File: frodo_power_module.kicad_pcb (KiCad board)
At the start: 2 copper layers, 55 x 71.2 mm, 39 parts, among them J1 Keystone 1098, J10 SWD Header, J2 Molex MicroFit 2x2, J3 Molex MicroFit 2x2, J4 Molex MicroFit 2x2, J5 Molex MicroFit 2x2, J6 Molex MicroFit 2x2, J7 JST-GH, J8 JST-GH, J9 JST-GH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

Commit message: Update PCB
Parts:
- removed SW1, SW2: EVQ-PUC02K, Button_Switch_SMD:Panasonic_EVQPUL_EVQPUC
- added C12: 1u, Capacitor_SMD:C_0805_2012Metric, B.Cu at (124.5, 114.5)
- added C13: 1u, Capacitor_SMD:C_0805_2012Metric, B.Cu at (124.5, 117.5)
- added C14: 100n, Capacitor_SMD:C_0603_1608Metric, B.Cu at (133.0, 114.2)
- added C15: 100n, Capacitor_SMD:C_0603_1608Metric, B.Cu at (133.0, 116.8)
- added C16: 100n, Capacitor_SMD:C_0603_1608Metric, B.Cu at (133.0, 119.3)
- added C17: 100n, Capacitor_SMD:C_0603_1608Metric, B.Cu at (133.0, 121.8)
- added JP1: SolderJumper_2_Open, Jumper:SolderJumper-2_P1.3mm_Open_RoundedPad1.0x1.5mm, B.Cu at (128.8, 114.8)
- added JP2: SolderJumper_2_Open, Jumper:SolderJumper-2_P1.3mm_Open_RoundedPad1.0x1.5mm, B.Cu at (128.8, 118.3)
- added JP3: SolderJumper_2_Open, Jumper:SolderJumper-2_P1.3mm_Open_RoundedPad1.0x1.5mm, B.Cu at (128.8, 121.9)
- added R10: 0, Resistor_SMD:R_0603_1608Metric, B.Cu at (110.3, 109.0)
- added R11: 10k, Resistor_SMD:R_0603_1608Metric, B.Cu at (110.3, 111.5)
- added R12: 10k, Resistor_SMD:R_0603_1608Metric, B.Cu at (110.3, 114.0)
- added R13: TODO, Resistor_SMD:R_2512_6332Metric, B.Cu at (110.3, 116.5)
- added R14: 100, Resistor_SMD:R_0603_1608Metric, B.Cu at (110.3, 119.0)
- added R15: 160, Resistor_SMD:R_0603_1608Metric, B.Cu at (106.3, 109.0)
- added R16: 260, Resistor_SMD:R_0603_1608Metric, B.Cu at (106.3, 111.5)
- added R17: 100, Resistor_SMD:R_0603_1608Metric, B.Cu at (106.3, 114.0)
- added R5: 100k, Resistor_SMD:R_0603_1608Metric, B.Cu at (114.3, 109.0)
- added R6: 4.7k, Resistor_SMD:R_0603_1608Metric, B.Cu at (114.3, 111.5)
- added R7: 1k, Resistor_SMD:R_0603_1608Metric, B.Cu at (114.3, 114.0)
- added R8: 1k, Resistor_SMD:R_0603_1608Metric, B.Cu at (114.3, 116.5)
- added R9: DNP, Resistor_SMD:R_0603_1608Metric, B.Cu at (114.3, 119.0)
- added TH1: NCU18XH103F6SRB, Resistor_SMD:R_0603_1608Metric, B.Cu at (133.0, 124.3)
- H1, H2, H3, H4: value MountingHole_3.2mm_M3_Pad_Via -> MountingHole_Pad
- moved C7 14.6 mm to (110.0, 134.0)
- moved U1 11.9 mm to (146.2, 109.6)
- moved U5 10.8 mm to (140.0, 136.8)
- moved C8 8.32 mm to (118.8, 109.5)
- moved C10 8.32 mm to (118.8, 114.5)
- moved C11 8.32 mm to (118.8, 117.0)
- moved C9 8.32 mm to (118.8, 112.0)
- moved L1 8.32 mm to (118.8, 119.5)
- moved R3 8.32 mm to (118.8, 122.0)
- moved R4 8.32 mm to (118.8, 124.5)
- moved Y1 6.37 mm to (139.2, 129.3)
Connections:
- net +12V renamed VDC
- C1 pad 2: +BATT -> +VSW
- H1 pad 1: (no net) -> GND
- H2 pad 1: (no net) -> GND
- H3 pad 1: (no net) -> GND
- H4 pad 1: (no net) -> GND
- J1 pad 1: +BATT -> BATT_RAW
- U2 pad 1: +BATT -> +VSW
- U4 pad 1: unconnected-(U4-IN-Pad1) -> Net-(D1-K)
- U4 pad 10: unconnected-(U4-OUT-Pad10) -> +BATT
- U4 pad 11: Net-(U4-GND-Pad11) -> GND
- U4 pad 2: unconnected-(U4-ISET-Pad2) -> Net-(U4-ISET)
- U4 pad 3: unconnected-(U4-~{CE}-Pad3) -> CHARGE_ENABLE
- U4 pad 4: unconnected-(U4-TS-Pad4) -> NTC
- U4 pad 5: Net-(U4-GND-Pad11) -> GND
- U4 pad 6: unconnected-(U4-CHM_TMR-Pad6) -> Net-(U4-CHM_TMR)
- U4 pad 7: unconnected-(U4-STAT1-Pad7) -> STAT1
- U4 pad 8: unconnected-(U4-STAT2-Pad8) -> STAT2
- U4 pad 9: unconnected-(U4-VSET-Pad9) -> Net-(U4-VSET)
- U5 pad 1: unconnected-(U5-VC2-Pad1) -> Net-(U5-VC2)
- U5 pad 2: unconnected-(U5-VC1-Pad2) -> Net-(U5-VC1)
- U5 pad 3: unconnected-(U5-VC1_CB-Pad3) -> Net-(U5-VC1_CB)
- U5 pad 4: unconnected-(U5-CD-Pad4) -> Net-(U5-CD)
- U5 pad 5: Net-(U5-GND) -> GND
- U5 pad 6: unconnected-(U5-~{CB_EN}-Pad6) -> GND
- U5 pad 7: unconnected-(U5-VDD-Pad7) -> Net-(U5-VDD)
- U5 pad 8: unconnected-(U5-OUT-Pad8) -> BLNCR_OUT
- U5 pad 9: Net-(U5-GND) -> GND

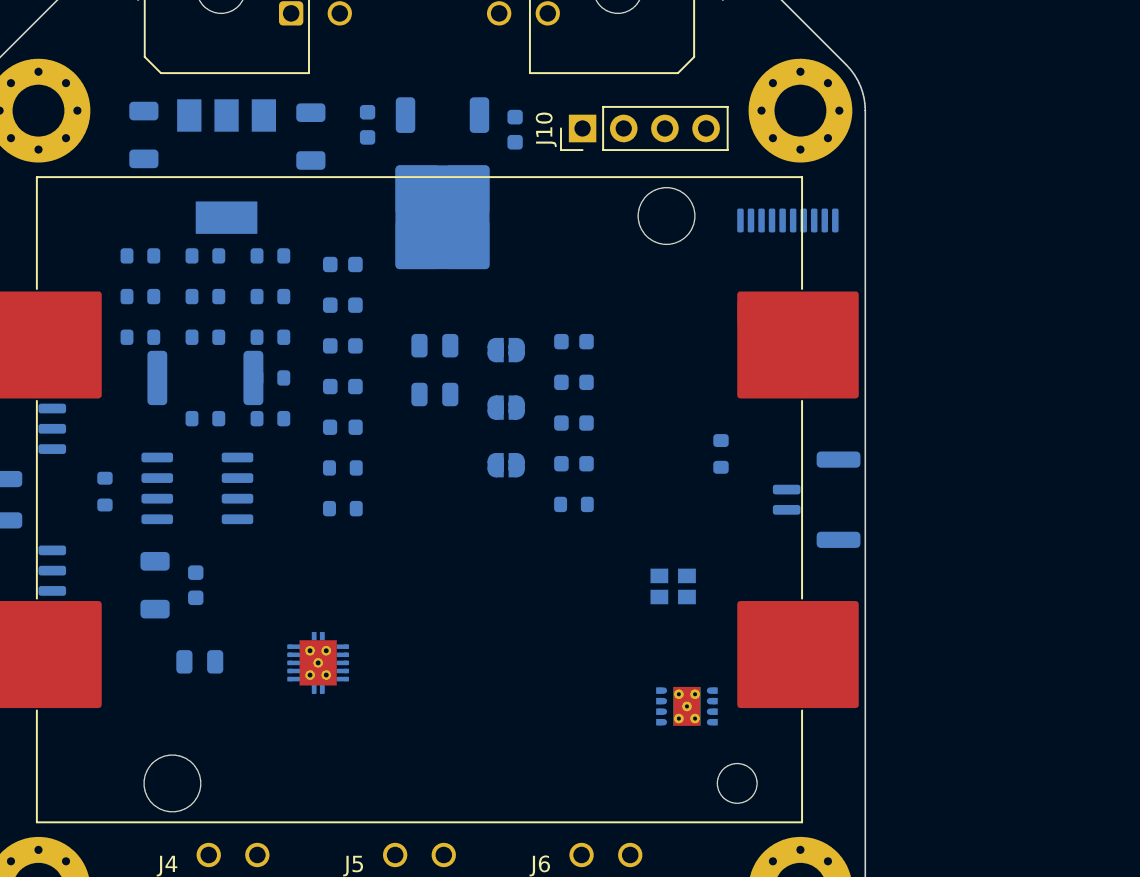
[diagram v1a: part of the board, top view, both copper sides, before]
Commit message: created component groups on pcb
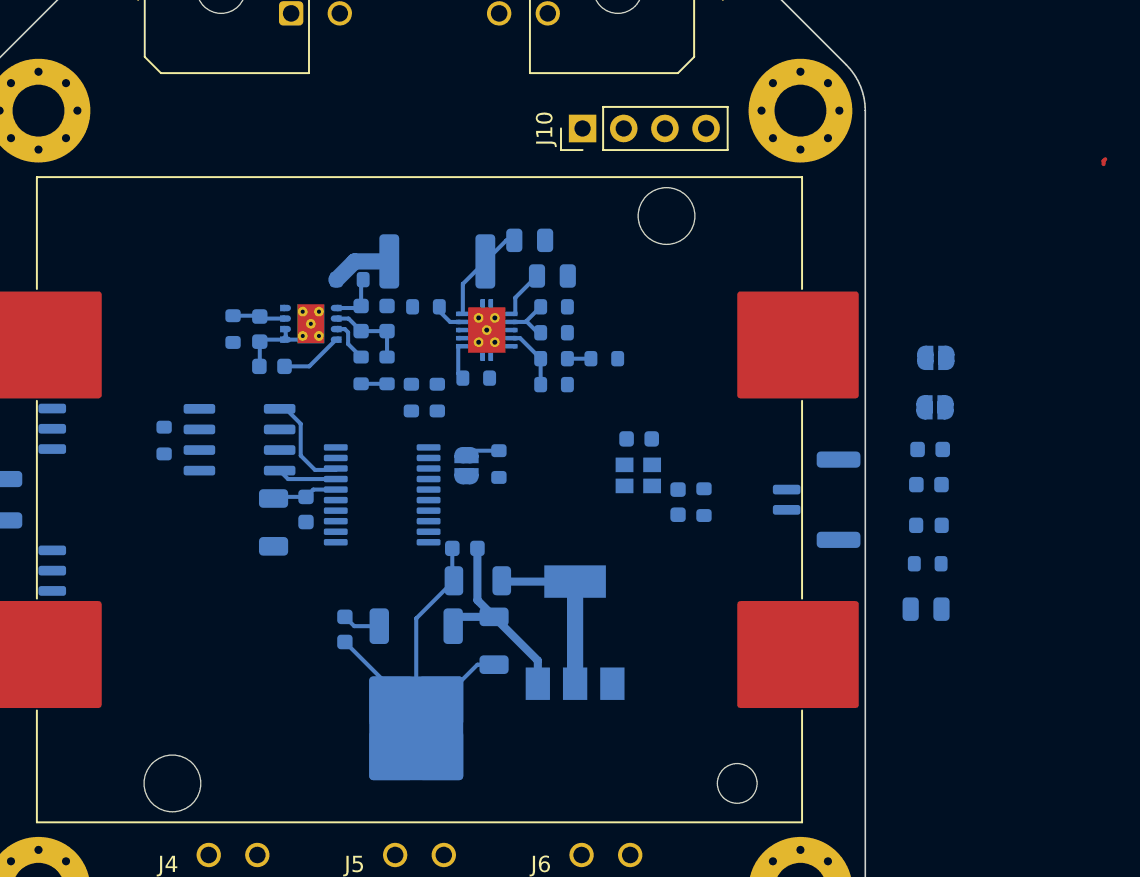
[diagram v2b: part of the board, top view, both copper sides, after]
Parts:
- R6: value 4.7k -> 3.6k
- moved C7 44.9 mm to (154.8, 130.8)
- moved C8 38.0 mm to (155.0, 120.9)
- moved C11 36.7 mm to (154.9, 123.1)
- moved L1 36.7 mm to (154.9, 125.6)
- moved U3 35.9 mm to (133.1, 132.2), turned to 90 degrees
- moved C4 34.4 mm to (127.1, 129.0), turned to 0 degrees
- moved U5 33.1 mm to (116.8, 113.2)
- moved C3 33.1 mm to (128.1, 132.7)
- moved U2 31.6 mm to (123.3, 136.8)
- moved C1 31.2 mm to (118.9, 132.0)
- moved U1 28.7 mm to (121.2, 123.7), turned to 180 degrees
- moved JP1 26.5 mm to (155.3, 115.2)
- moved JP2 26.5 mm to (155.3, 118.3)
- moved C2 26.0 mm to (126.3, 127.0), turned to 0 degrees
- moved C9 24.0 mm to (139.4, 124.2), turned to 90 degrees
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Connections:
- U1 pad 10: unconnected-(U1-PA4-Pad10) -> BREAKWIRE
- U1 pad 11: unconnected-(U1-PA5-Pad11) -> NTC
- U1 pad 6: unconnected-(U1-PA0-Pad6) -> STAT1
- U1 pad 7: unconnected-(U1-PA1-Pad7) -> STAT2
- U1 pad 8: unconnected-(U1-PA2-Pad8) -> CHARGE_ENABLE
- U1 pad 9: unconnected-(U1-PA3-Pad9) -> BLNCR_OUT
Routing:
- net GND: track 0.00 -> 27.5 mm
- net +3V3: track 0.00 -> 14.9 mm
- net +5V: track 0.00 -> 12.7 mm
- net CAN_TX: track 0.00 -> 6.26 mm
- net +BATT: track 0.00 -> 6.14 mm
- net Net-(U5-VC1): track 0.00 -> 4.87 mm
- net Net-(U5-CD): track 0.00 -> 4.06 mm
- net BATT_RAW: track 0.00 -> 3.73 mm
- net NTC: track 0.00 -> 3.69 mm
- net CAN_RX: track 0.00 -> 3.68 mm
- net Net-(U4-ISET): track 0.00 -> 3.13 mm
- net Net-(U5-VDD): track 0.00 -> 3.12 mm
- net Net-(U5-VC2): track 0.00 -> 3.08 mm
- net Net-(D1-K): track 0.00 -> 2.89 mm
- net Net-(U5-VC1_CB): track 0.00 -> 2.69 mm
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
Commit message: Add current sense amp to PCB
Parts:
- added C18: 100n, Capacitor_SMD:C_0603_1608Metric, B.Cu at (165.0, 138.0)
- added C19: 100n, Capacitor_SMD:C_0603_1608Metric, B.Cu at (165.0, 140.5)
- added C20: 100n, Capacitor_SMD:C_0603_1608Metric, B.Cu at (118.5, 117.0)
- added R18: 10k, Resistor_SMD:R_0603_1608Metric, B.Cu at (121.0, 116.3)
- added R19: 10k, Resistor_SMD:R_0603_1608Metric, B.Cu at (121.0, 113.0)
- added R20: 1k8, Resistor_SMD:R_0603_1608Metric, B.Cu at (161.0, 138.0)
- added R21: 1k, Resistor_SMD:R_0603_1608Metric, B.Cu at (161.0, 140.5)
- added R22: 1k8, Resistor_SMD:R_0603_1608Metric, B.Cu at (161.0, 143.0)
- added R23: 1k, Resistor_SMD:R_0603_1608Metric, B.Cu at (161.0, 145.5)
- added R24: 1k8, Resistor_SMD:R_0603_1608Metric, B.Cu at (128.5, 111.2)
- added U7: INA213, Package_TO_SOT_SMD:SOT-363_SC-70-6, B.Cu at (118.8, 114.5)
- R13: value TODO -> 5m
- R15: value 160 -> 120
- R16: value 260 -> 220
- R6: value 3.6k -> 1k8
- R7, R8: value 1k -> 220
- moved C10 28.4 mm to (115.7, 138.8)
- moved R3 28.4 mm to (119.7, 142.8)
- moved Y1 28.4 mm to (115.6, 141.1)
- moved C9 28.4 mm to (118.0, 142.8)
- moved R15 9.53 mm to (110.3, 113.9)
- moved U5 8.54 mm to (109.0, 116.6)
- moved C15 8.43 mm to (112.2, 116.3)
- moved R17 8.43 mm to (112.2, 119.5)
- moved C16 8.43 mm to (113.8, 116.3)
- moved R16 8.43 mm to (113.8, 119.5)
- moved C14 8.40 mm to (106.0, 117.0)
- moved C17 8.40 mm to (106.8, 119.2)
- moved C2 8.24 mm to (134.5, 127.5)
- moved U2 8.24 mm to (131.5, 137.3)
- moved C3 8.24 mm to (136.3, 133.2)
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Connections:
- net BATT_RAW renamed Net-(J1-Pin_1)
- C12 pad 1: Net-(D1-K) -> VDC
- J2 pad 3: VDC -> Net-(D1-A)
- J2 pad 4: VDC -> Net-(D1-A)
- JP1 pad 1: Net-(D1-K) -> VDC
- R6 pad 2: GND -> Net-(R24-Pad1)
- R7 pad 2: GND -> Net-(R7-Pad2)
- R8 pad 1: Net-(U4-ISET) -> Net-(R7-Pad2)
- U1 pad 12: unconnected-(U1-PA6-Pad12) -> VSENSE_CHARGE
- U1 pad 13: unconnected-(U1-PA7-Pad13) -> VSENSE_BATT
- U1 pad 14: unconnected-(U1-PB1-Pad14) -> ISENSE
- U4 pad 1: Net-(D1-K) -> VDC
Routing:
- net BLNCR_OUT: track 0.00 -> 13.7 mm
- net Net-(J1-Pin_1): track 3.73 -> 15.9 mm, vias 0 -> 12
- net ISENSE: track 0.00 -> 9.87 mm
- net +BATT: track 6.14 -> 12.4 mm
- net +3V3: track 14.9 -> 20.6 mm
- net Net-(U7-REF): track 0.00 -> 3.21 mm
- net VDC: track 0.00 -> 2.89 mm
- net Net-(D1-K): track 2.89 -> 0.00 mm
- net GND: track 27.5 -> 29.3 mm, vias 0 -> 20
- net Net-(R24-Pad1): track 0.00 -> 1.75 mm
- net Net-(U5-VC2): track 3.08 -> 3.60 mm
- added copper zone on B.Cu, net +BATT
- added copper zone on B.Cu, net GND
- added copper zone on F.Cu, net GND
- added copper zone on B.Cu, net Net-(J1-Pin_1)
- added copper zone on F.Cu, net Net-(J1-Pin_1)
- added copper zone on F.Cu, net Net-(J1-Pin_2)
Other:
- board size 55 x 71.2 mm -> 56 x 71.2 mm
- board text added: "TODOs: - Silkscreen - Infos for Connectors - Name & rev - JLCJLCJLCJLC"

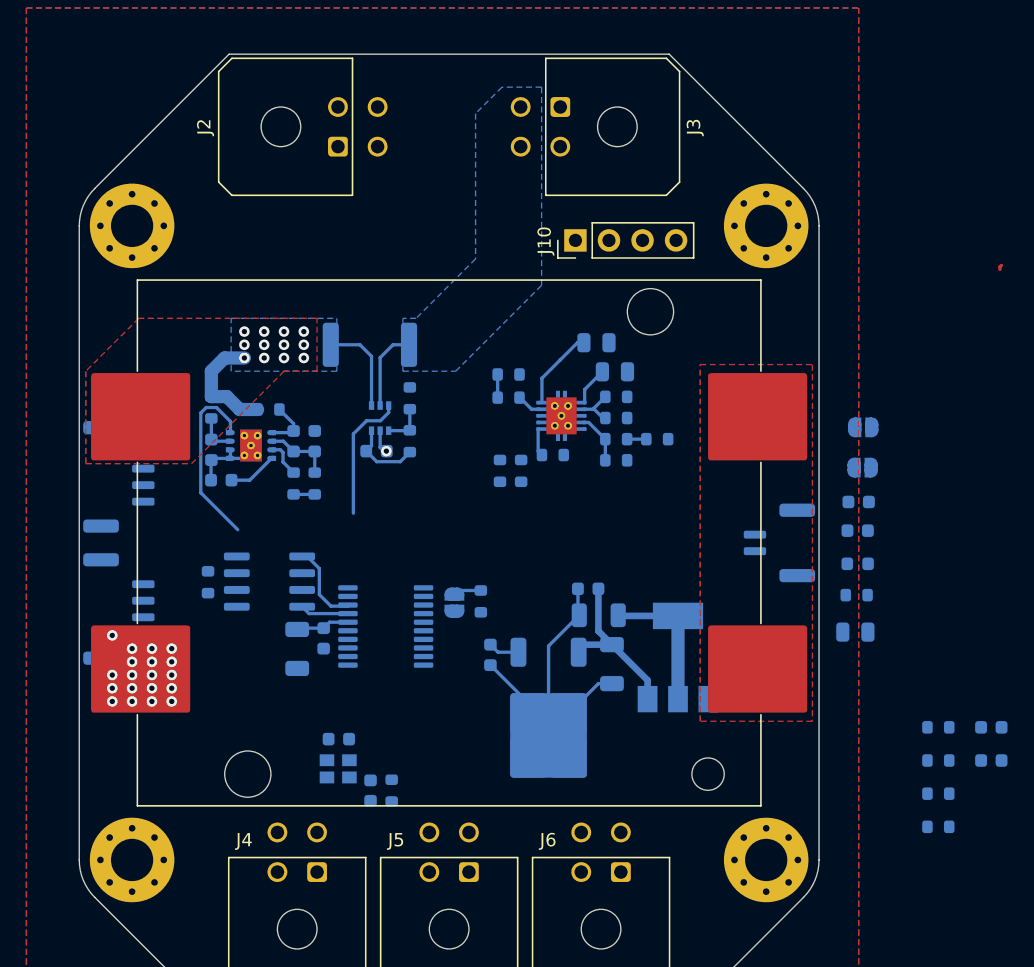
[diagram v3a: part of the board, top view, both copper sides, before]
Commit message: changed PCB
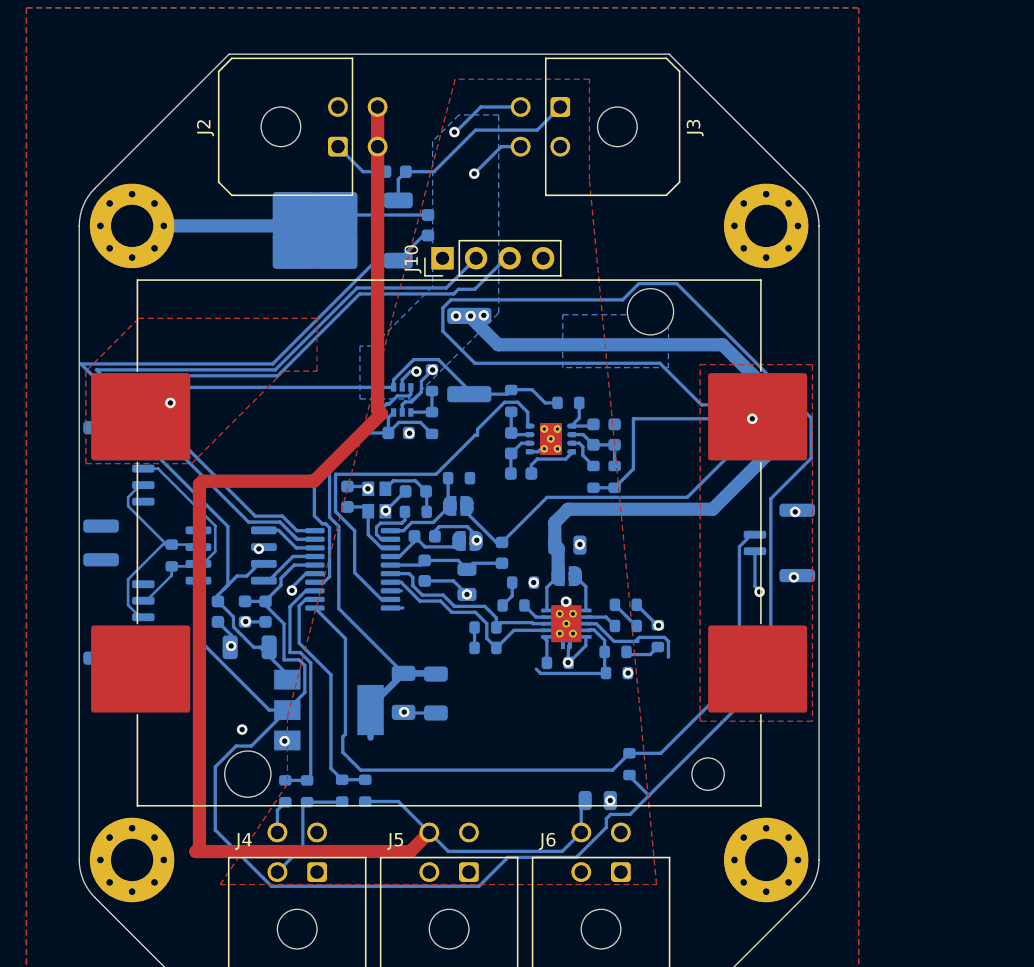
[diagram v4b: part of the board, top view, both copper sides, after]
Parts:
- R20: value 1k8 -> 5k1
- moved C19 59.6 mm to (106.5, 129.2), turned to 90 degrees
- moved C18 55.6 mm to (110.1, 129.2), turned to 90 degrees
- moved R22 49.4 mm to (111.6, 142.8), turned to 90 degrees
- moved R23 47.9 mm to (113.2, 142.8), turned to -90 degrees
- moved R21 45.2 mm to (115.9, 142.8), turned to -90 degrees
- moved R20 43.6 mm to (117.7, 142.8), turned to 90 degrees
- moved U2 40.4 mm to (115.1, 100.3), turned to 180 degrees
- moved C1 37.3 mm to (120.0, 95.9), turned to 0 degrees
- moved C8 33.3 mm to (122.2, 126.1), turned to 90 degrees
- moved C11 32.8 mm to (122.2, 123.5)
- moved C12 32.5 mm to (135.2, 143.5)
- moved JP2 30.4 mm to (125.4, 123.8), turned to 0 degrees
- moved C2 30.1 mm to (122.4, 100.0), turned to -90 degrees
- moved C7 29.6 mm to (125.3, 127.0), turned to 90 degrees
- moved C3 27.5 mm to (108.9, 131.9), turned to 0 degrees
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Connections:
- J2 pad 3: Net-(D1-A) -> VDC
- J2 pad 4: Net-(D1-A) -> VDC
- JP1 pad 1: VDC -> Net-(D1-K)
- U1 pad 10: BREAKWIRE -> CHARGE_ENABLE
- U1 pad 11: NTC -> BREAKWIRE
- U1 pad 6: STAT1 -> STAT2
- U1 pad 7: STAT2 -> STAT1
- U1 pad 8: CHARGE_ENABLE -> NTC
- U4 pad 1: VDC -> Net-(D1-K)
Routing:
- net +3V3: track 20.6 -> 244.9 mm
- net VDC: track 2.89 -> 106.8 mm
- net +BATT: track 12.4 -> 70.8 mm, vias 0 -> 6
- net BREAKWIRE: track 0.00 -> 57.6 mm
- net SWDIO: track 0.00 -> 54.5 mm
- net SWCLK: track 0.00 -> 53.6 mm
- net +5V: track 12.7 -> 66.1 mm
- net GND: track 29.3 -> 75.4 mm, vias 20 -> 23
- net VSENSE_BATT: track 0.00 -> 18.4 mm
- net VSENSE_CHARGE: track 0.00 -> 17.6 mm
- net Net-(J1-Pin_1): track 15.9 -> 32.8 mm, vias 12 -> 1
- net CAN+: track 0.00 -> 16.7 mm
- net CAN-: track 0.00 -> 16.6 mm
- net BLNCR_OUT: track 13.7 -> 30.0 mm
- net +VSW: track 2.36 -> 18.7 mm
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- added copper zone on F.Cu, net +VSW
